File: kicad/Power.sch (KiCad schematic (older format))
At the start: 26 parts, among them Q1 BC848B, Q2 Si2301BDS, Q3 Si2301BDS, U1 Buck_Converter, U2 TMR_3-1221

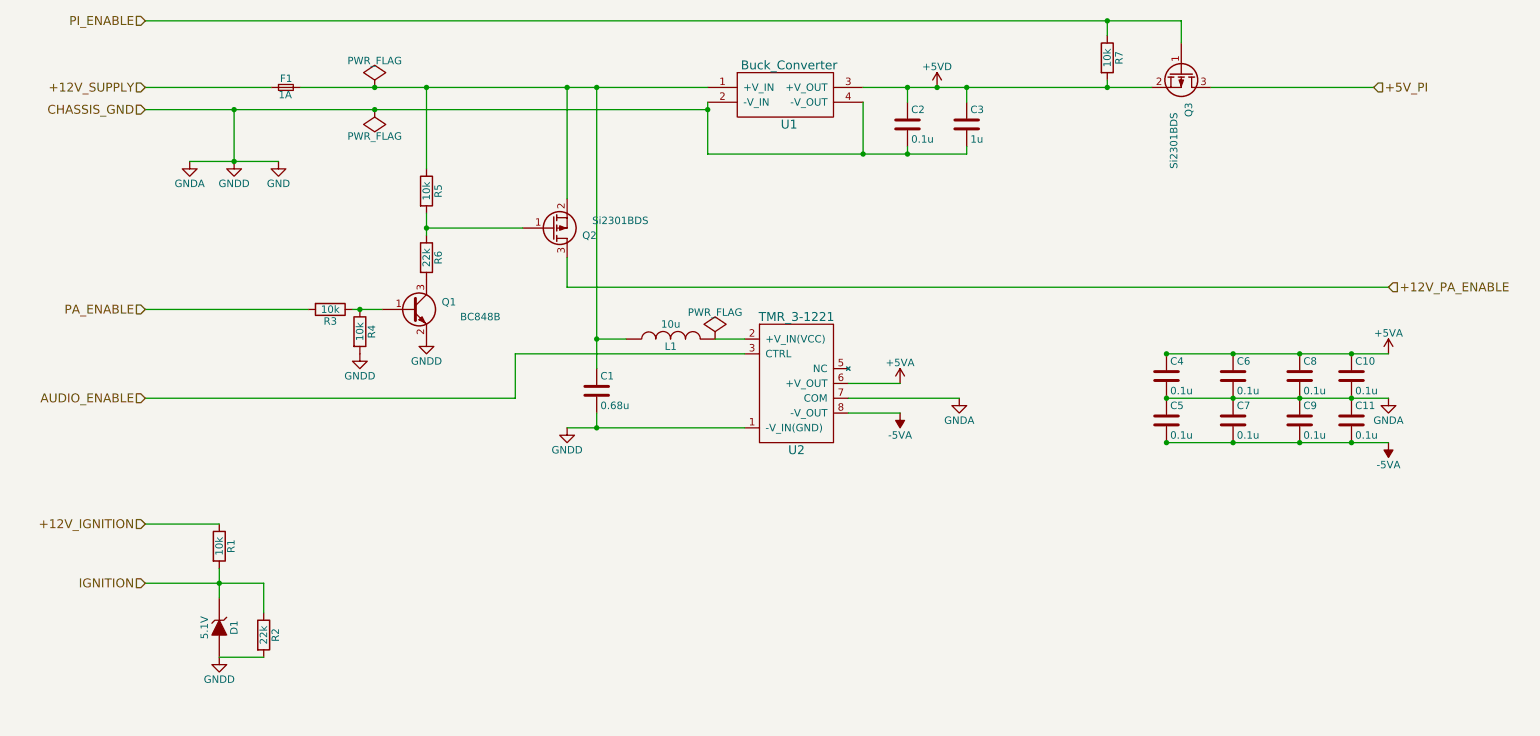
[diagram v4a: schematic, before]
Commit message: Updated to include extra indicator LEDs controlled by the ATMega.  PCB reworked
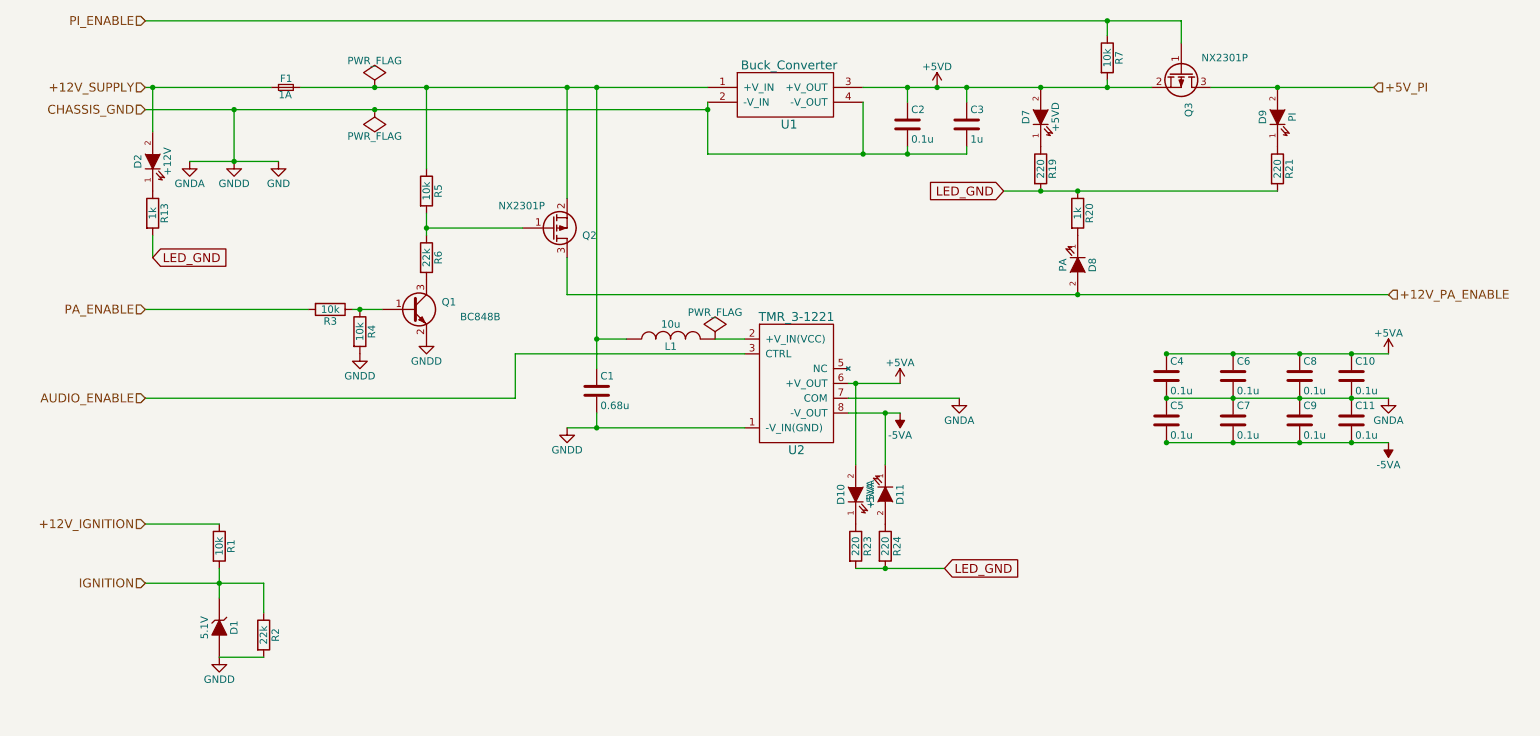
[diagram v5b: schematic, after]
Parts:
- added D10: +5VA, SMD_LED:LED_SMD_1.6x0.8mm, symbol LED
- added D11: -5VA, SMD_LED:LED_SMD_1.6x0.8mm, symbol LED
- added D2: +12V, SMD_LED:LED_SMD_1.6x0.8mm, symbol LED
- added D7: +5VD, SMD_LED:LED_SMD_1.6x0.8mm, symbol LED
- added D8: PA, SMD_LED:LED_SMD_1.6x0.8mm, symbol LED
- added D9: PI, SMD_LED:LED_SMD_1.6x0.8mm, symbol LED
- added R13, R20: 1k, Resistors_SMD:R_0603_HandSoldering, symbol R
- added R19, R21, R23, R24: 220, Resistors_SMD:R_0603_HandSoldering, symbol R
- L1: footprint Inductors:SELF-WE-PD3S -> Inductor_SRR0735A:Inductor_SRR0735A
- Q2, Q3: value Si2301BDS -> NX2301P
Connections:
- net +12V_PA_ENABLE: now also D8.2 (A)
- net +12V_SUPPLY: now also D2.2 (A)
- net +5VA: now also D10.2 (A)
- net +5VD: now also D7.2 (A)
- net +5V_PI: now also D9.2 (A)
- net -5VA: now also D11.1 (K)
- new net: D7.1 (K), R19.1
- new net: D9.1 (K), R21.1
- new net: D8.1 (K), R20.2
- new net: D2.1 (K), R13.1
- new net: D10.1 (K), R23.1
- new net: D11.2 (A), R24.1
- new net LED_GND: R13.2, R19.2, R20.1, R21.2, R23.2, R24.2
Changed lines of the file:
@@
 F 0 "L1" V 5200 3050 50  0000 C CNN
 F 1 "10u" V 5350 3050 50  0000 C CNN
-F 2 "Inductors:SELF-WE-PD3S" H 5250 3050 50  0001 C CNN
+F 2 "Inductor_SRR0735A:Inductor_SRR0735A" H 5250 3050 50  0001 C CNN
 F 3 "" H 5250 3050 50  0000 C CNN
 	1    5250 3050
@@
 Text HLabel 10000 1350 2    60   Input ~ 0
 +5V_PI
-Text HLabel 10100 2700 2    60   Input ~ 0
+Text HLabel 10100 2750 2    60   Input ~ 0
 +12V_PA_ENABLE
 $Comp
@@
 P 8700 1250
 F 0 "Q3" H 9000 1300 50  0000 R CNN
-F 1 "Si2301BDS" H 9350 1200 50  0000 R CNN
+F 1 "NX2301P" V 8600 1700 50  0000 R CNN
 F 2 "TO_SOT_Packages_SMD:SOT-23_Handsoldering" H 8900 1350 50  0001 C CNN
 F 3 "" H 8700 1250 50  0000 C CNN
@@
 	0    1    1    0
 $EndComp
-Wire Wire Line
-	8900 1350 10000 1350
 $Comp
 L +5VD #PWR012
@@
 P 4450 2300
 F 0 "Q2" H 4750 2350 50  0000 R CNN
-F 1 "Si2301BDS" H 5100 2250 50  0000 R CNN
+F 1 "NX2301P" H 4400 2150 50  0000 R CNN
 F 2 "TO_SOT_Packages_SMD:SOT-23_Handsoldering" H 4650 2400 50  0001 C CNN
 F 3 "" H 4450 2300 50  0000 C CNN
@@
 	2750 1350 5500 1350
 Connection ~ 3250 1350
-Wire Wire Line
-	6550 1350 8500 1350
 Connection ~ 7050 1350
 $Comp
@@
 Connection ~ 8200 900
 Wire Wire Line
-	8200 1300 8200 1350
+	8200 1350 8200 1300
 Connection ~ 8200 1350
 $Comp
@@
 	4200 3150 5750 3150
 Wire Wire Line
-	4550 2500 4550 2700
-Wire Wire Line
-	4550 2700 10100 2700
+	4550 2500 4550 2750
 Wire Wire Line
 	4750 3050 4950 3050
 Connection ~ 4750 1350
+$Comp
+L LED D7
+U 1 1 5762DC7B
+P 7750 1550
+F 0 "D7" H 7750 1650 50  0000 C CNN
+F 1 "+5VD" H 7750 1450 50  0000 C CNN
+F 2 "SMD_LED:LED_SMD_1.6x0.8mm" H 7750 1550 50  0001 C CNN
+F 3 "" H 7750 1550 50  0000 C CNN
+	1    7750 1550
+	0    -1   -1   0
+$EndComp
+$Comp
+L LED D9
+U 1 1 5762DD1B
+P 9350 1550
+F 0 "D9" H 9350 1650 50  0000 C CNN
+F 1 "PI" H 9350 1450 50  0000 C CNN
+F 2 "SMD_LED:LED_SMD_1.6x0.8mm" H 9350 1550 50  0001 C CNN
+F 3 "" H 9350 1550 50  0000 C CNN
+	1    9350 1550
+	0    -1   -1   0
+$EndComp
+$Comp
+L LED D8
+U 1 1 5762DD8D
+P 8000 2550
+F 0 "D8" H 8000 2650 50  0000 C CNN
+F 1 "PA" H 8000 2450 50  0000 C CNN
+F 2 "SMD_LED:LED_SMD_1.6x0.8mm" H 8000 2550 50  0001 C CNN
+F 3 "" H 8000 2550 50  0000 C CNN
+	1    8000 2550
+	0    1    1    0
+$EndComp
+$Comp
+L LED D2
+U 1 1 5762DDFA
+P 1750 1850
+F 0 "D2" H 1750 1950 50  0000 C CNN
+F 1 "+12V" H 1750 1750 50  0000 C CNN
+F 2 "SMD_LED:LED_SMD_1.6x0.8mm" H 1750 1850 50  0001 C CNN
+F 3 "" H 1750 1850 50  0000 C CNN
+	1    1750 1850
+	0    -1   -1   0
+$EndComp
+$Comp
+L R R21
+U 1 1 5762DE7D
+P 9350 1900
+F 0 "R21" V 9430 1900 50  0000 C CNN
+F 1 "220" V 9350 1900 50  0000 C CNN
+F 2 "Resistors_SMD:R_0603_HandSoldering" V 9280 1900 50  0001 C CNN
+F 3 "" H 9350 1900 50  0000 C CNN
+	1    9350 1900
+	1    0    0    -1
+$EndComp
+$Comp
+L R R19
+U 1 1 5762DF8E
+P 7750 1900
+F 0 "R19" V 7830 1900 50  0000 C CNN
+F 1 "220" V 7750 1900 50  0000 C CNN
+F 2 "Resistors_SMD:R_0603_HandSoldering" V 7680 1900 50  0001 C CNN
+F 3 "" H 7750 1900 50  0000 C CNN
+	1    7750 1900
+	1    0    0    -1
+$EndComp
+$Comp
+L R R20
+U 1 1 5762E06C
+P 8000 2200
+F 0 "R20" V 8080 2200 50  0000 C CNN
+F 1 "1k" V 8000 2200 50  0000 C CNN
+F 2 "Resistors_SMD:R_0603_HandSoldering" V 7930 2200 50  0001 C CNN
+F 3 "" H 8000 2200 50  0000 C CNN
+	1    8000 2200
+	1    0    0    -1
+$EndComp
+$Comp
+L R R13
+U 1 1 5762E184
+P 1750 2200
+F 0 "R13" V 1830 2200 50  0000 C CNN
+F 1 "1k" V 1750 2200 50  0000 C CNN
+F 2 "Resistors_SMD:R_0603_HandSoldering" V 1680 2200 50  0001 C CNN
+F 3 "" H 1750 2200 50  0000 C CNN
+	1    1750 2200
+	1    0    0    -1
+$EndComp
+Text GLabel 7500 2050 0    60   Input ~ 0
+LED_GND
+Connection ~ 7750 2050
+Text GLabel 1750 2500 2    60   Input ~ 0
+LED_GND
+Wire Wire Line
+	1750 1350 1750 1650
+Connection ~ 1750 1350
+Wire Wire Line
+	1750 2350 1750 2500
+Wire Wire Line
+	4550 2750 10100 2750
+Connection ~ 8000 2750
+Wire Wire Line
+	7500 2050 9350 2050
+Connection ~ 8000 2050
+$Comp
+L LED D10
+U 1 1 5762F2D2
+P 6500 4100
+F 0 "D10" H 6500 4200 50  0000 C CNN
+F 1 "+5VA" H 6500 4000 50  0000 C CNN
+F 2 "SMD_LED:LED_SMD_1.6x0.8mm" H 6500 4100 50  0001 C CNN
+F 3 "" H 6500 4100 50  0000 C CNN
+	1    6500 4100
+	0    -1   -1   0
+$EndComp
+$Comp
+L LED D11
+U 1 1 5762F36B
+P 6700 4100
+F 0 "D11" H 6700 4200 50  0000 C CNN
+F 1 "-5VA" H 6700 4000 50  0000 C CNN
+F 2 "SMD_LED:LED_SMD_1.6x0.8mm" H 6700 4100 50  0001 C CNN
+F 3 "" H 6700 4100 50  0000 C CNN
+	1    6700 4100
+	0    1    1    0
+$EndComp
+$Comp
+L R R23
+U 1 1 5762F3E7
+P 6500 4450
+F 0 "R23" V 6580 4450 50  0000 C CNN
+F 1 "220" V 6500 4450 50  0000 C CNN
+F 2 "Resistors_SMD:R_0603_HandSoldering" V 6430 4450 50  0001 C CNN
+F 3 "" H 6500 4450 50  0000 C CNN
+	1    6500 4450
+	1    0    0    -1
+$EndComp
+$Comp
+L R R24
+U 1 1 5762F47D
+P 6700 4450
+F 0 "R24" V 6780 4450 50  0000 C CNN
+F 1 "220" V 6700 4450 50  0000 C CNN
+F 2 "Resistors_SMD:R_0603_HandSoldering" V 6630 4450 50  0001 C CNN
+F 3 "" H 6700 4450 50  0000 C CNN
+	1    6700 4450
+	1    0    0    -1
+$EndComp
+Wire Wire Line
+	6500 3900 6500 3350
+Connection ~ 6500 3350
+Wire Wire Line
+	6700 3900 6700 3550
+Connection ~ 6700 3550
+Text GLabel 7100 4600 2    60   Input ~ 0
+LED_GND
+Wire Wire Line
+	6550 1350 8500 1350
+Connection ~ 7750 1350
+Wire Wire Line
+	8900 1350 10000 1350
+Connection ~ 9350 1350
+Wire Wire Line
+	6500 4600 7100 4600
+Connection ~ 6700 4600
 $EndSCHEMATC
